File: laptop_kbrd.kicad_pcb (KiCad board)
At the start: 2 copper layers, 58 parts, among them CON1 AVR-ISP-6-DR, Q1 MOSFET_N, Q2 MOSFET_N, Q3 MOSFET_N, Q4 MOSFET_N, Q5 MOSFET_N, Q6 MOSFET_N, Q7 MOSFET_N, Q8 ALS_PT19, SW1 MCU_RST, SW2 BT_ASSCN, SW3 POWER, U1 ATMEGA32U4-AU, U2 RT9706, U3 RCLAMP0502B

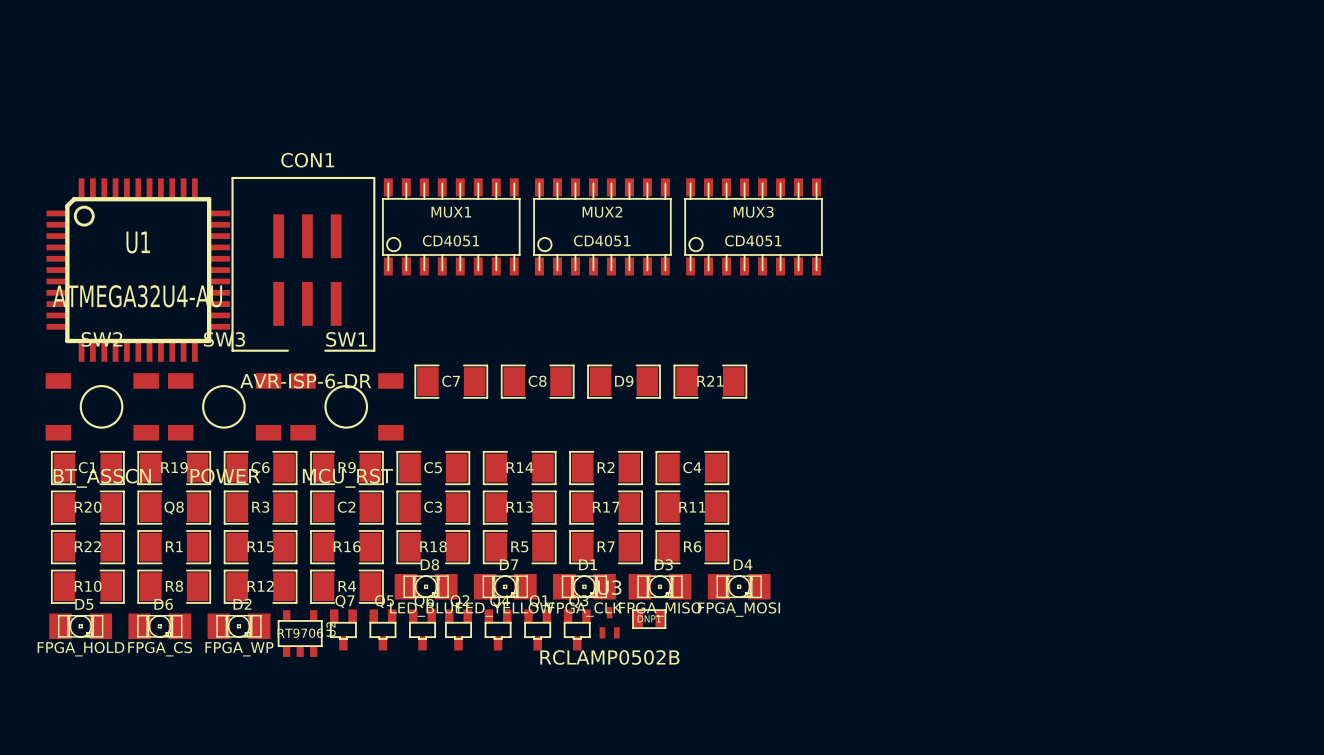
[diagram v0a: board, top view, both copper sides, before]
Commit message: All footprints done. Hopefully, FPC header has right parity.
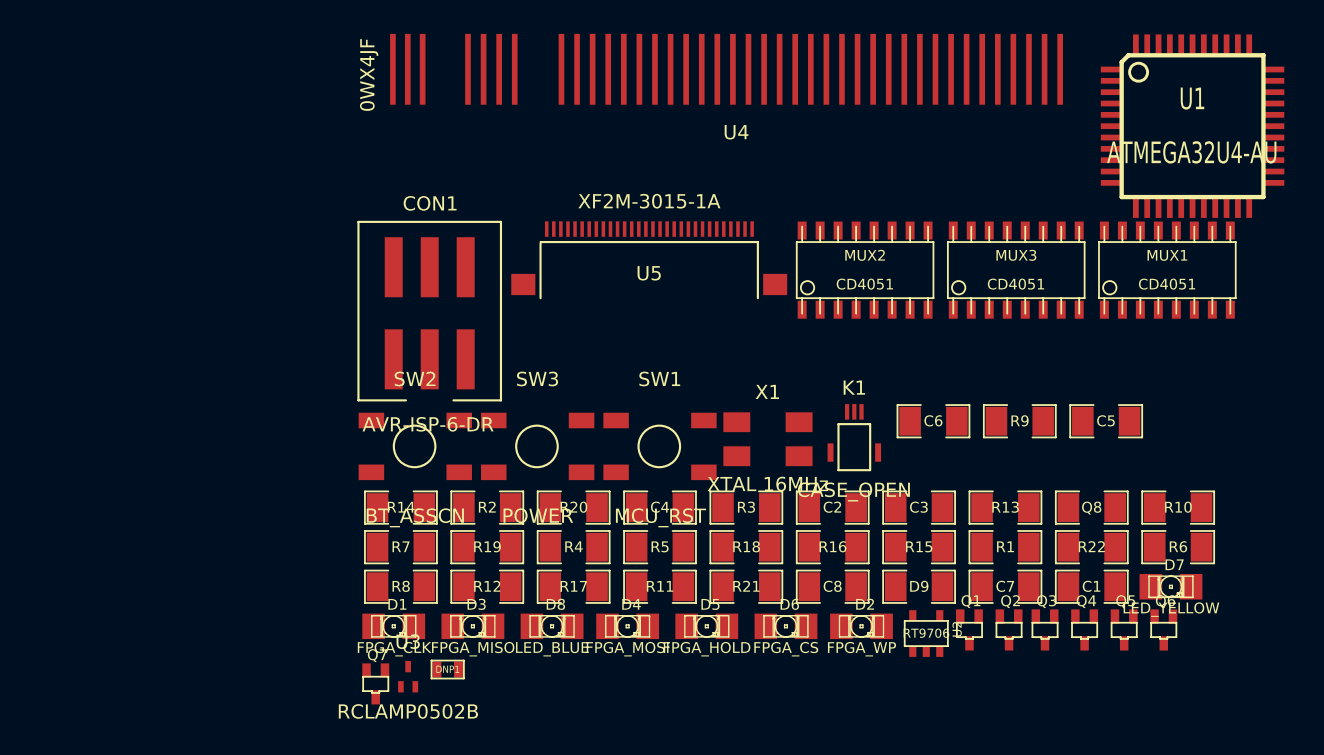
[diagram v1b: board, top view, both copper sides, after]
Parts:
- added K1: CASE_OPEN, 3pin_FPC, F.Cu at (28.2, 8.64)
- added U4: 0WX4JF, 0WXJ4F, F.Cu at (19.8, -17.0)
- added U5: XF2M-3015-1A, XF2M_3015_1A, F.Cu at (13.7, -5.84)
- added X1: XTAL 16MHz, XTAL_6mmx3.5mm, F.Cu at (22.1, 8.89)
- Q1, Q2, Q3, Q4, Q5, Q6, Q7: footprint SOT323 -> SOT323_DR
- Q8: footprint SM1206 -> SM1206_ALS
- moved R10 77.2 mm to (51.1, 13.7)
- moved U1 75.1 mm to (52.1, -13.2)
- moved C1 71.4 mm to (45.0, 19.3)
- moved R22 70.9 mm to (45.0, 16.5)
- moved Q8 64.8 mm to (45.0, 13.7)
- moved R1 58.7 mm to (38.9, 16.5)
- moved Q5 52.3 mm to (47.2, 22.4)
- moved Q6 52.3 mm to (50.0, 22.4)
- moved MUX1 50.6 mm to (50.3, -3.05)
- moved C5 47.6 mm to (46.0, 7.62)
- moved C6 47.6 mm to (33.8, 7.62)
- moved R9 47.6 mm to (39.9, 7.62)
- moved D7 47.0 mm to (50.5, 19.3)
- moved R15 46.5 mm to (32.8, 16.5)
- moved D5 44.2 mm to (17.8, 22.1)
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
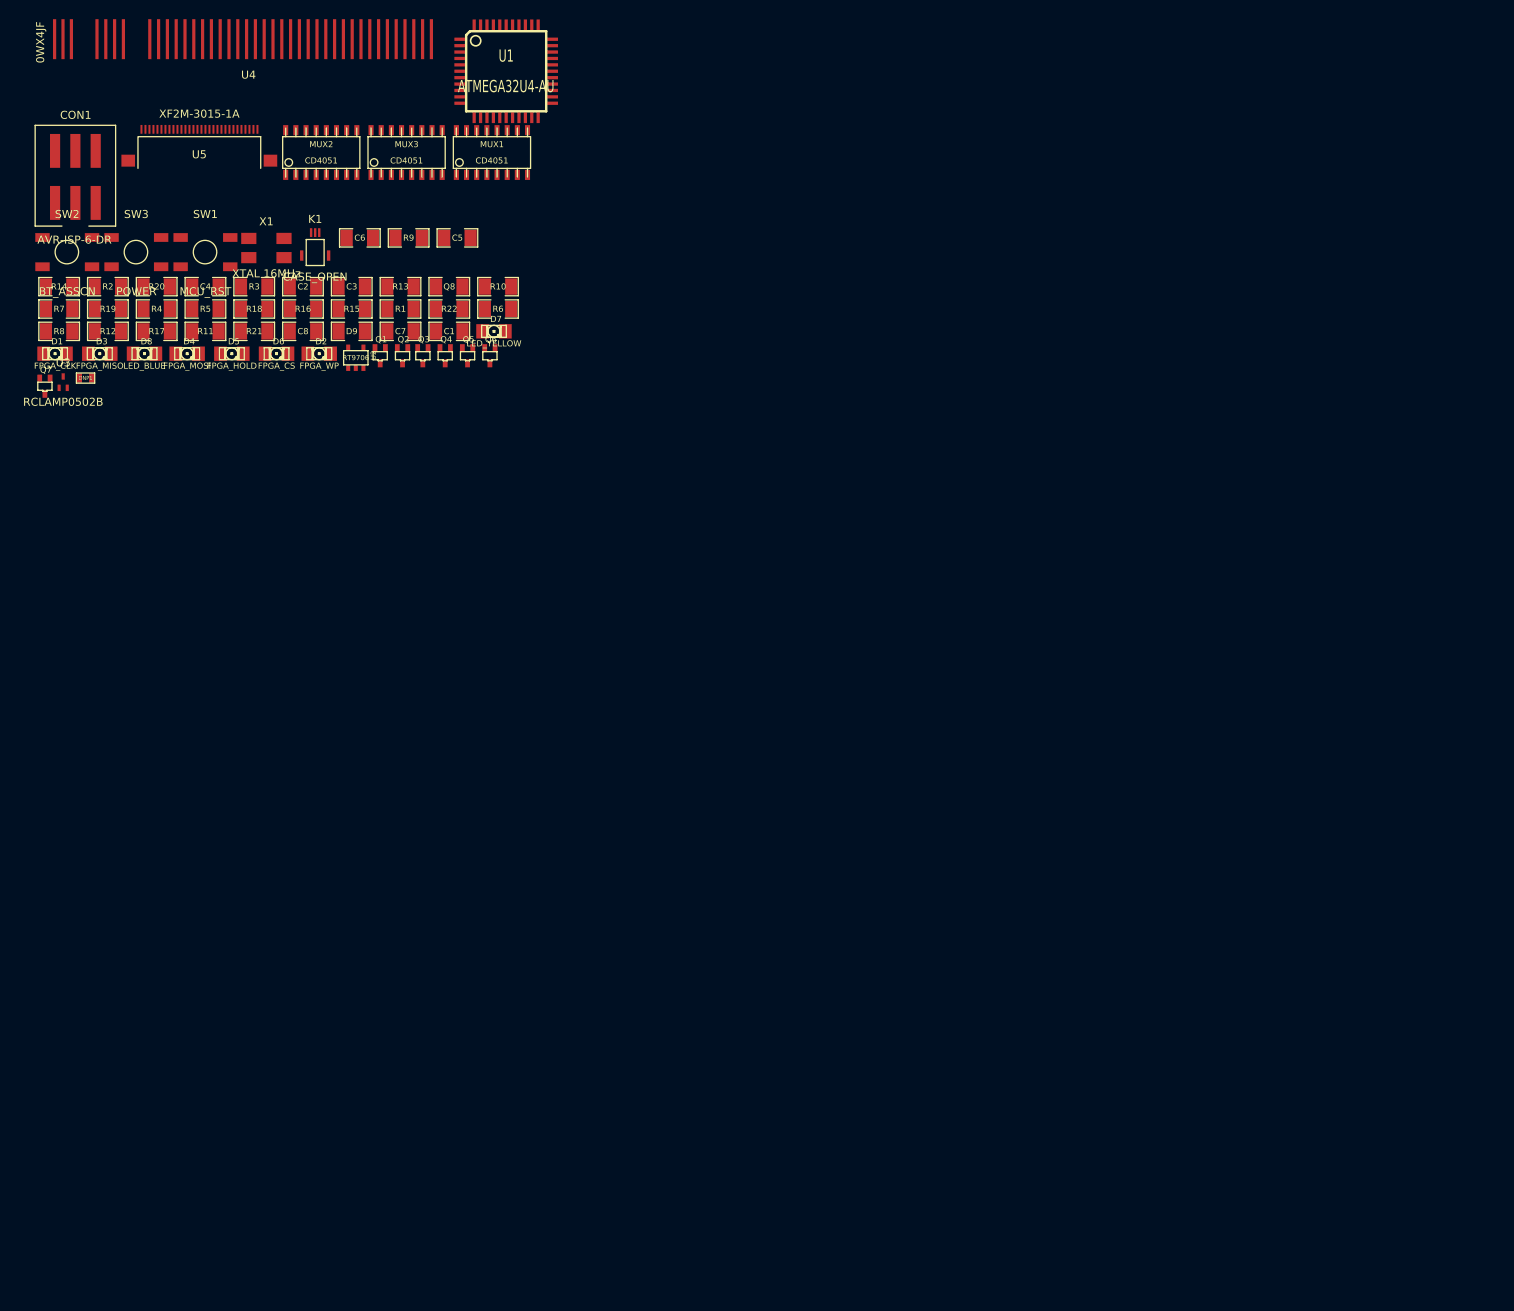
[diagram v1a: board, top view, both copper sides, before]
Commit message: We'll need to do something about track clearances in PCB.
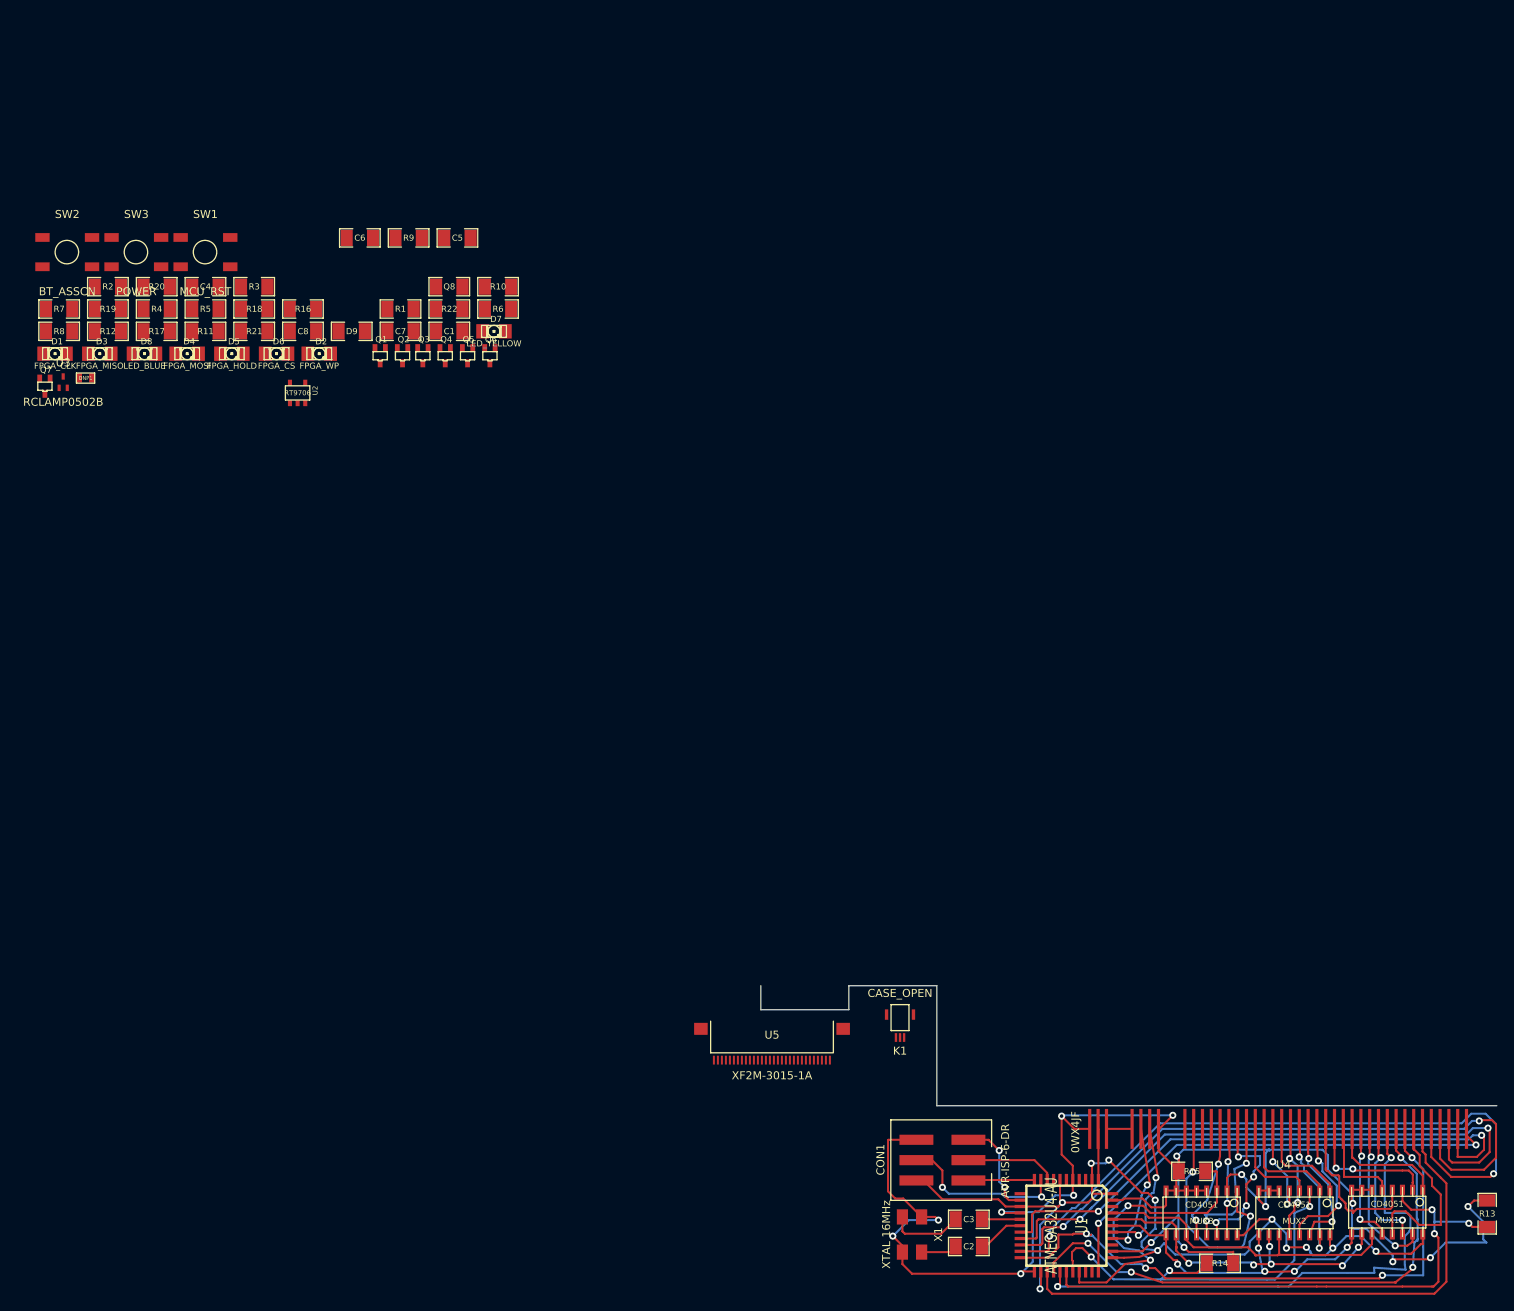
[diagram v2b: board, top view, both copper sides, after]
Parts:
- U2: footprint SOT23-5 -> SOT23-5_DR
- moved R14 189.6 mm to (141.3, 135.8)
- moved U4 187.9 mm to (149.2, 119.2)
- moved MUX2 179.9 mm to (150.6, 129.5), turned to 180 degrees
- moved R13 178.6 mm to (174.7, 129.6), turned to 90 degrees
- moved MUX1 173.4 mm to (162.2, 129.4), turned to 180 degrees
- moved MUX3 165.7 mm to (139.0, 129.5), turned to 180 degrees
- moved CON1 163.9 mm to (106.6, 122.9), turned to 90 degrees
- moved U1 160.4 mm to (122.1, 131.1), turned to 270 degrees
- moved R15 150.5 mm to (137.8, 124.3), turned to 180 degrees
- moved X1 147.4 mm to (102.8, 132.2), turned to 270 degrees
- moved C2 146.0 mm to (109.9, 133.7)
- moved C3 139.8 mm to (109.9, 130.3)
- moved U5 136.4 mm to (85.3, 110.3), turned to 180 degrees
- moved K1 121.7 mm to (101.3, 105.9), turned to 180 degrees
- moved U2 8.50 mm to (26.0, 27.0)
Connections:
- MUX2 pad 8: (no net) -> GND
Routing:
- net GND: track 0.00 -> 235.7 mm, vias 0 -> 16
- net VCC: track 0.00 -> 123.3 mm, vias 0 -> 11
- net /P5: track 0.00 -> 87.2 mm, vias 0 -> 2
- net /P4: track 0.00 -> 83.2 mm, vias 0 -> 2
- net /P3: track 0.00 -> 78.3 mm, vias 0 -> 2
- net /P8: track 0.00 -> 74.4 mm, vias 0 -> 4
- net /P6: track 0.00 -> 73.3 mm
- net /P2: track 0.00 -> 73.0 mm, vias 0 -> 2
- net /COM1: track 0.00 -> 70.4 mm, vias 0 -> 3
- net /P9: track 0.00 -> 68.8 mm, vias 0 -> 4
- net /P10: track 0.00 -> 68.8 mm, vias 0 -> 2
- net /P1: track 0.00 -> 59.8 mm, vias 0 -> 2
- net /COM2: track 0.00 -> 50.0 mm, vias 0 -> 3
- net /B: track 0.00 -> 42.1 mm, vias 0 -> 6
- net /C: track 0.00 -> 41.7 mm, vias 0 -> 5
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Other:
- board outline added: 92 x 15 mm

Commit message: Should I remove RCLAMP?
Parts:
- D1, D2, D3, D4, D5, D6, D7, D8, Q8, SW1, SW2, SW3: moved to B.Cu
- moved R20 203.3 mm to (172.9, 133.2), turned to 180 degrees
- moved Q8 166.6 mm to (156.1, 137.8), turned to 180 degrees
- moved D1 153.6 mm to (149.0, 31.3)
- moved R2 148.3 mm to (149.0, 35.2)
- moved C4 147.1 mm to (116.6, 119.6), turned to 90 degrees
- moved SW1 145.3 mm to (108.6, 120.1)
- moved SW2 143.1 mm to (72.1, 131.3), turned to 90 degrees
- moved SW3 141.0 mm to (103.4, 111.2)
- moved D8 140.8 mm to (72.2, 146.8)
- moved R7 140.6 mm to (135.5, 35.2)
- moved C8 139.1 mm to (72.1, 150.8)
- moved R4 136.6 mm to (142.3, 43.5)
- moved R8 134.6 mm to (128.6, 43.5)
- moved D3 134.4 mm to (135.4, 31.3)
- moved R3 133.5 mm to (96.9, 123.2), turned to 90 degrees
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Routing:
- net /TS_ANA: track 0.00 -> 118.8 mm, vias 0 -> 2
- net /5V_DELAYED: track 0.00 -> 107.2 mm, vias 0 -> 3
- net GND: track 235.7 -> 320.2 mm, vias 16 -> 21
- net VDD: track 3.20 -> 47.1 mm, vias 0 -> 2
- net /D-: track 0.00 -> 42.7 mm, vias 0 -> 2
- net /D+: track 0.00 -> 42.5 mm, vias 0 -> 2
- net /3.3V_DELAYED: track 0.00 -> 33.7 mm, vias 0 -> 2
- net /RST: track 12.6 -> 37.9 mm, vias 2 -> 3
- net VCC: track 123.3 -> 148.2 mm, vias 11 -> 15
- net /KEY_COL3: track 0.00 -> 22.0 mm, vias 0 -> 2
- net /CHG_PWRSWITCH: track 0.00 -> 19.0 mm, vias 0 -> 1
- net /GPT_CMPOUT3: track 0.00 -> 15.5 mm, vias 0 -> 2
- net /FPGA CLK: track 0.00 -> 13.3 mm, vias 0 -> 4
- net /FPGA MISO: track 0.00 -> 13.3 mm, vias 0 -> 1
- net /FPGA MOSI: track 0.00 -> 12.4 mm, vias 0 -> 1
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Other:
- board size 92 x 15 mm -> 111.5 x 18 mm
- net class Default: clearance 0.254 -> 0.153
- rule trace_clearance: 0.254 -> 0.153
- rule trace_min: 0.254 -> 0.153
